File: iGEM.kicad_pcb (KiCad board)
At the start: 4 copper layers, 98 x 98 mm, 63 parts, among them IC1 TMCS1107A1BQDRQ1, IC2 MCP4642-502E_UN, IC3 SN74LVC2G08IDCTRQ1, IC4 NLSX4373DR2G, J1 COIL, J2 Conn_01x03, J3 Conn_01x02, J4 Conn_01x04, J5 Conn_01x03, J6 Conn_02x03_Odd_Even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

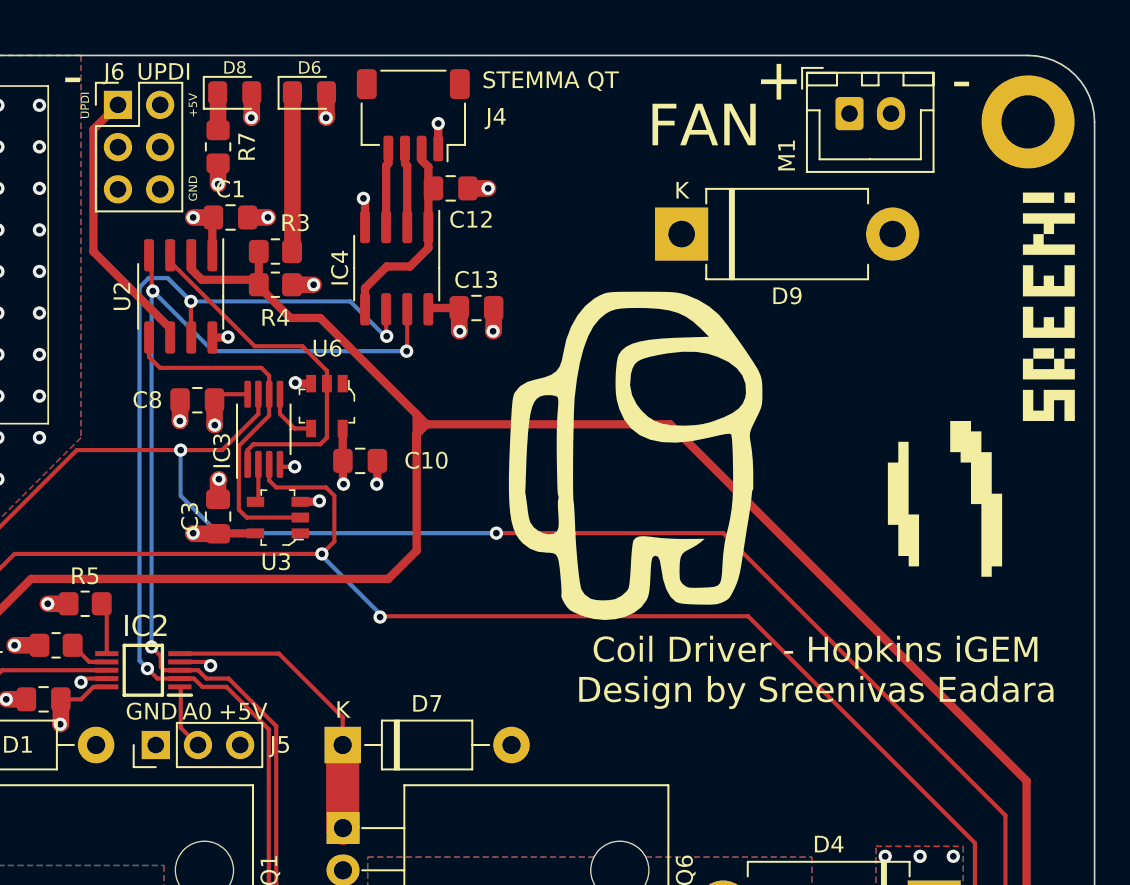
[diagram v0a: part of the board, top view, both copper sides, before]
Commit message: updated to include programming power protection and cleanup
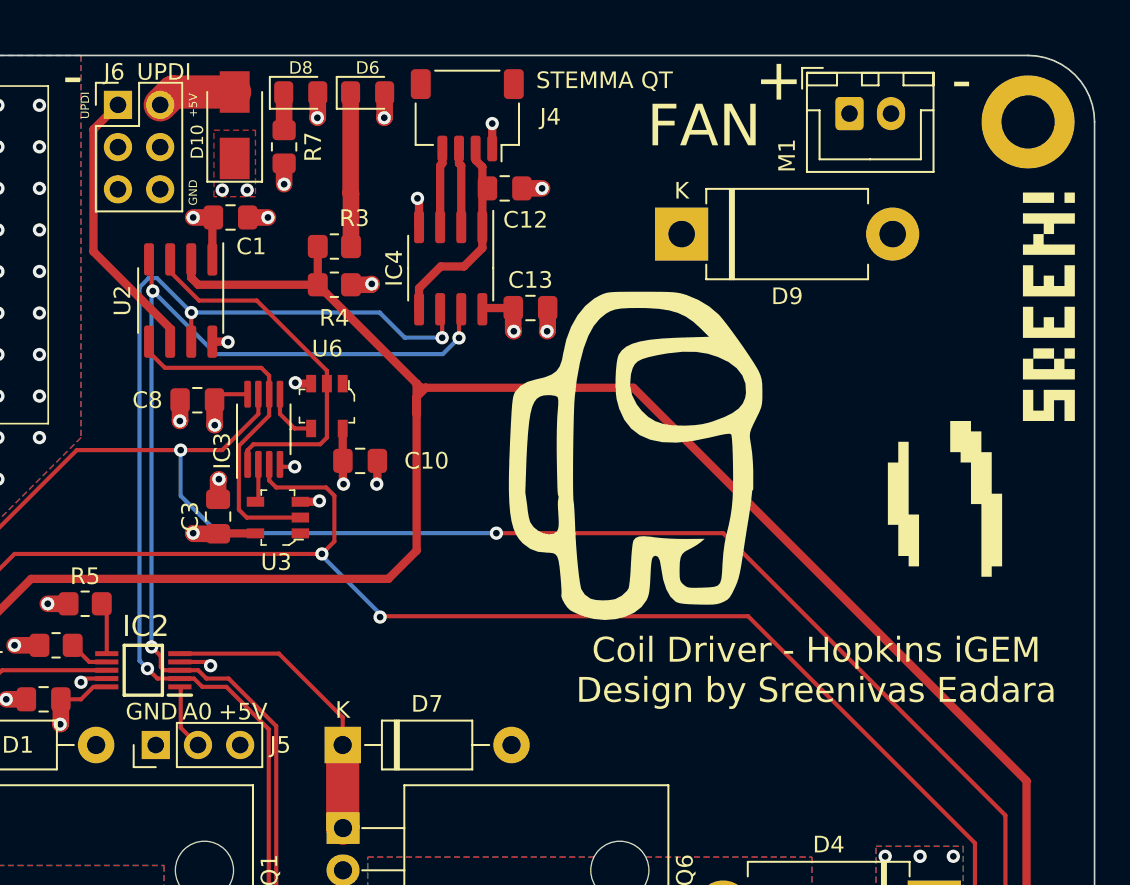
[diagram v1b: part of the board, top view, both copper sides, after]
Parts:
- added D10: B130-E3, Diode_SMD:D_SMA, F.Cu at (109.2, 51.2)
- moved D8 3.97 mm to (113.2, 49.2)
- moved R7 3.97 mm to (112.2, 52.5)
- moved R3 3.56 mm to (115.2, 58.5)
- moved R4 3.55 mm to (115.2, 60.8)
- moved D6 3.50 mm to (117.2, 49.2)
- moved C12 3.25 mm to (125.5, 55.0)
- moved C13 3.25 mm to (127.0, 62.2)
- moved IC4 3.25 mm to (122.2, 59.8)
- moved J4 3.25 mm to (123.2, 50.6)
- moved U2 0.25 mm to (106.0, 61.8)
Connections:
- J6 pad 2: +5V -> Net-(D10-Pad2)
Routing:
- net Net-(D10-Pad2): track 0.00 -> 4.81 mm
- net SCL: track 84.7 -> 87.6 mm
- net SDA: track 82.5 -> 85.2 mm
- net ENABLE: track 169.3 -> 171.5 mm
- net PWM2: track 21.6 -> 20.5 mm
- net VCC: track 12.5 -> 11.6 mm
- net +5V: track 41.6 -> 41.9 mm, vias 74 -> 76

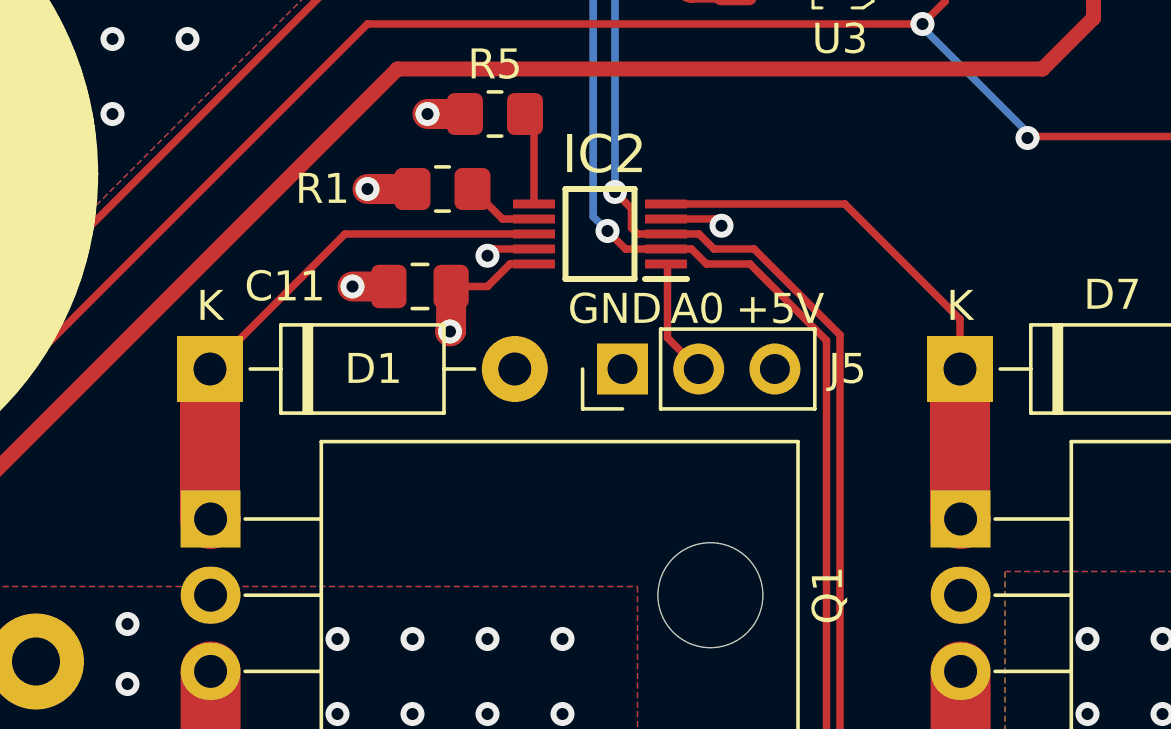
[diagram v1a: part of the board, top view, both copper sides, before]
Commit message: Improved copper balance and cleanup
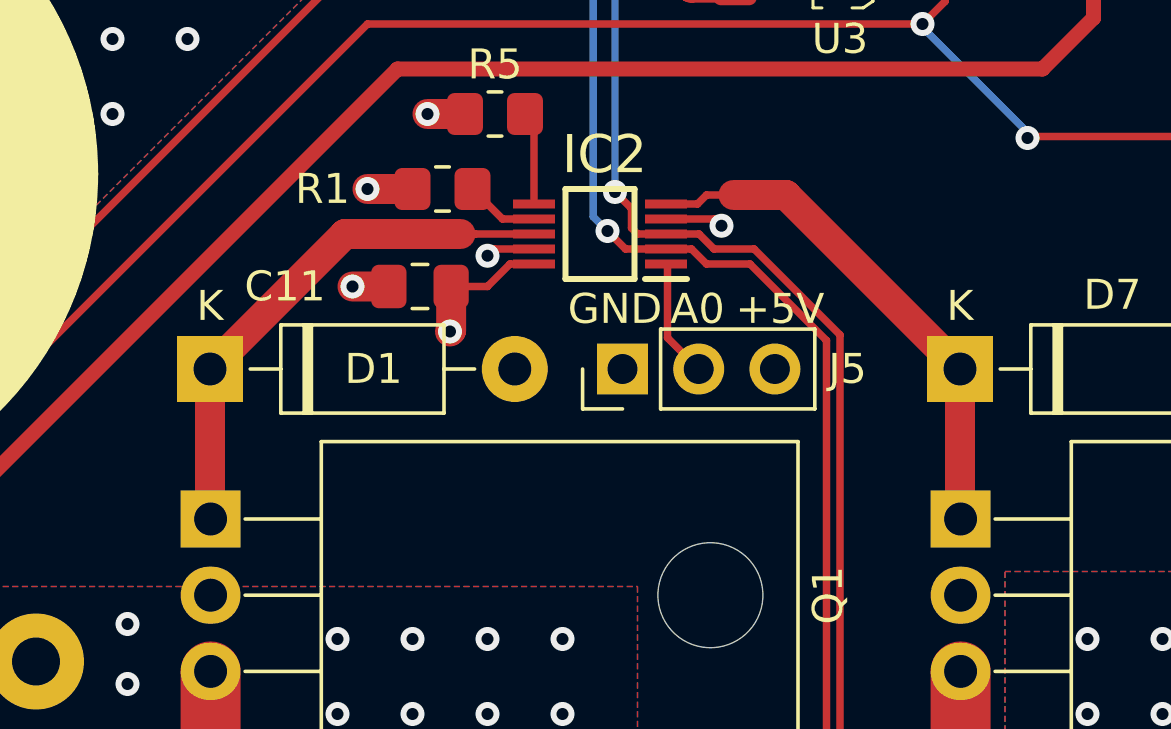
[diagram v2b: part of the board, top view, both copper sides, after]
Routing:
- net RHEO2_OUT: track 18.1 -> 17.3 mm
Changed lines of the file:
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@@
   (via (at 76 121.5) (size 0.8) (drill 0.4) (layers "F.Cu" "B.Cu") (free) (net 2))
   (via (at 97.5 70) (size 0.8) (drill 0.4) (layers "F.Cu" "B.Cu") (free) (net 2))
-  (segment (start 90.75 88.5) (end 90.75 93.48) (width 2) (layer "F.Cu") (net 3))
-  (segment (start 95.25 84) (end 90.75 88.5) (width 0.25) (layer "F.Cu") (net 3))
-  (segment (start 101.55 84) (end 95.25 84) (width 0.25) (layer "F.Cu") (net 3))
-  (segment (start 90.75 93.48) (end 90.77 93.5) (width 2) (layer "F.Cu") (net 3))
+  (segment (start 99.1 84) (end 95.25 84) (width 1) (layer "F.Cu") (net 3))
+  (segment (start 99.6 84) (end 99.1 84) (width 0.25) (layer "F.Cu") (net 3))
+  (segment (start 95.25 84) (end 90.75 88.5) (width 1) (layer "F.Cu") (net 3))
+  (segment (start 90.75 88.5) (end 90.75 93.48) (width 1) (layer "F.Cu") (net 3))
+  (segment (start 101.55 84) (end 99.6 84) (width 0.25) (layer "F.Cu") (net 3))
   (via (at 80 122.5) (size 0.8) (drill 0.4) (layers "F.Cu" "B.Cu") (free) (net 4))
   (via (at 77.5 132.5) (size 0.8) (drill 0.4) (layers "F.Cu" "B.Cu") (free) (net 4))
@@
   (segment (start 116.225 49.25) (end 116.225 55.275) (width 1) (layer "F.Cu") (net 8))
   (segment (start 116.25 55.3) (end 116.25 58.5) (width 1) (layer "F.Cu") (net 8))
-  (segment (start 111.911299 83) (end 115.75 86.838701) (width 0.25) (layer "F.Cu") (net 9))
-  (segment (start 115.75 88.5) (end 115.75 93.48) (width 2) (layer "F.Cu") (net 9))
-  (segment (start 115.75 93.48) (end 115.77 93.5) (width 2) (layer "F.Cu") (net 9))
-  (segment (start 115.75 86.838701) (end 115.75 88.5) (width 0.25) (layer "F.Cu") (net 9))
-  (segment (start 105.95 83) (end 111.911299 83) (width 0.25) (layer "F.Cu") (net 9))
+  (segment (start 108.2 82.7) (end 109.95 82.7) (width 1) (layer "F.Cu") (net 9))
+  (segment (start 109.95 82.7) (end 115.75 88.5) (width 1) (layer "F.Cu") (net 9))
+  (segment (start 107.3 82.7) (end 107 83) (width 0.25) (layer "F.Cu") (net 9))
+  (segment (start 115.75 88.5) (end 115.75 93.48) (width 1) (layer "F.Cu") (net 9))
+  (segment (start 108.2 82.7) (end 107.3 82.7) (width 0.25) (layer "F.Cu") (net 9))
+  (segment (start 107 83) (end 105.95 83) (width 0.25) (layer "F.Cu") (net 9))
   (via (at 72.5 60) (size 0.8) (drill 0.4) (layers "F.Cu" "B.Cu") (free) (net 10))
   (via (at 77.5 65) (size 0.8) (drill 0.4) (layers "F.Cu" "B.Cu") (free) (net 10))

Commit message: Replace out of stock Stemma QT header
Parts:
- G***: moved to B.Cu
- J4: footprint Connector_JST:JST_SH_SM04B-SRSS-TB_1x04-1MP_P1.00mm_Horizontal -> Connector_JST:JST_XH_B4B-XH-A_1x04_P2.50mm_Vertical
- moved D9 17.9 mm to (154.1, 57.8), turned to 180 degrees
- moved G*** 15.5 mm to (149.4, 71.3), turned to -90 degrees
- moved J4 6.81 mm to (130.0, 51.5)
- moved C12 3.09 mm to (128.5, 55.8)
- moved M1 2.70 mm to (148.8, 51.5), turned to 180 degrees
- moved IC4 2.16 mm to (123.8, 58.2)
- moved C13 2.05 mm to (128.5, 60.8)
- moved G*** 0.56 mm to (154.2, 66.0)
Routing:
- net SDA: track 85.2 -> 87.8 mm
- net GND: track 36.3 -> 34.2 mm, vias 120 -> 119
- net VCC: track 11.6 -> 13.3 mm
- net SCL: track 87.6 -> 88.5 mm
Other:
- board text added: "Coil Driver Hopkins iGEM Sreeni Eadara"
- board text added: "I2C"
- board text added: "SCL"
- board text added: "SDA"
- board text added: "VCC"
- board text removed: "Coil Driver - Hopkins iGEM Design by Sreenivas Eadara"
- board text removed: "STEMMA QT"

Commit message: miscellaneous improvements and cleanup
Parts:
- moved C5 9.13 mm to (66.1, 111.0), turned to 180 degrees
- moved U1 6.94 mm to (108.3, 123.3), turned to 0 degrees
- moved C7 4.30 mm to (108.4, 117.3), turned to 0 degrees
- moved C4 2.27 mm to (108.0, 120.3), turned to 0 degrees
- moved U4 2.16 mm to (68.0, 105.9), turned to -90 degrees
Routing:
- net DIR1: track 162.8 -> 142.9 mm
- net DIR2: track 145.7 -> 129.5 mm
- net Net-(IC1-Pad7): track 16.6 -> 6.05 mm
- net Net-(J2-Pad2): track 7.69 -> 15.8 mm
- net SDA: track 87.8 -> 94.4 mm
- net SCL: track 88.5 -> 94.7 mm
- net FET3: track 12.4 -> 6.59 mm
- net FET1: track 7.75 -> 13.0 mm
- net ENABLE: track 171.5 -> 169.5 mm, vias 0 -> 2
- net +5V: track 41.9 -> 43.3 mm, vias 76 -> 73
- net GND: track 34.2 -> 35.2 mm
